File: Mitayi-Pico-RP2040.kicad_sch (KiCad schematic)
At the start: 53 parts, among them J1 EXP8, J2 USB_C_Receptacle_USB2.0, J3 Header_1, J4 Header_2, J5 SWD, J6 USB_B_Micro, SW1 Reset, SW2 UBUT, U1 W25Q128JVS, U2 MIC5219-3.3YM5, U3 RP2040, Y1 YIC-12M20P2/XT324-10/10

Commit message: Remove headers and much more
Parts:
- removed J1: EXP8, Connector_PinHeader_2.54mm:PinHeader_2x04_P2.54mm_Vertical, symbol Connector_Generic:Conn_02x04_Counter_Clockwise
- removed J3: Header_1, CIRCUITSTATE-Connector-Pin-Headers:PinHeader_1x20_2H_P2.54mm_Vertical, symbol Connector_Generic:Conn_01x20
- removed J4: Header_2, CIRCUITSTATE-Connector-Pin-Headers:PinHeader_1x20_2H_P2.54mm_Vertical, symbol Connector_Generic:Conn_01x20
- removed J5: SWD, Connector_PinHeader_2.54mm:PinHeader_1x03_P2.54mm_Vertical, symbol Connector_Generic:Conn_01x03
- removed J6: USB_B_Micro, Connector_USB:USB_Micro-B_Molex-105017-0001, symbol Connector:USB_B_Micro
- D1: footprint Diode_SMD:D_SOD-323_HandSoldering -> Diode_SMD:D_SOD-123F
- J2: JLC (none) -> C5337088
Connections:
- net +3V3: no longer U1.8 (VCC)
- net GND: no longer U1.4 (GND)
- net QSPI_SCLK: no longer U1.6 (CLK)
- net QSPI_SD0: no longer U1.5 (DI(IO0))
- net QSPI_SD1: no longer U1.2 (DO(IO1))
- net QSPI_SD2: no longer U1.3 (IO2)
- net QSPI_SD3: no longer U1.7 (IO3)
- net QSPI_SS: no longer U1.1 (~{CS})
- no-connect marks 3 -> 2
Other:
- note removed: "EXP8"
- note removed: "Headers"
- note removed: "Pads should be masked out if not using Micro-USB. Otherwise, USB-C connector will cause a short."
- note removed: "SWD"
- note removed: "USB Micro"
- moved on the sheet: U1

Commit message: Update footprints
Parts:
- J2: footprint CIRCUITSTATE_Connector_USB:Korean-Hroparts-Elec_TYPE-C-31-M-12 -> 00ProjectFootprints:Korean-Hroparts-Elec_TYPE-C-31-M-12
- U1: footprint Package_SO:SOIC-8_5.23x5.23mm_P1.27mm -> 00ProjectFootprints:SOIC-8_5.23x5.23mm_P1.27mm
- U3: footprint CIRCUITSTATE-QFN:RP2040-QFN-56 -> 00ProjectFootprints:RP2040-QFN-56
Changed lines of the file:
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@@
       (effects (font (size 0.8 0.8)))
     )
-    (property "Footprint" "CIRCUITSTATE_Connector_USB:Korean-Hroparts-Elec_TYPE-C-31-M-12" (at 240.792 96.52 0)
+    (property "Footprint" "00ProjectFootprints:Korean-Hroparts-Elec_TYPE-C-31-M-12" (at 240.792 96.52 0)
       (effects (font (size 0.8 0.8)) hide)
     )
@@
       (effects (font (size 0.8 0.8)))
     )
-    (property "Footprint" "Package_SO:SOIC-8_5.23x5.23mm_P1.27mm" (at 337.312 46.99 0)
+    (property "Footprint" "00ProjectFootprints:SOIC-8_5.23x5.23mm_P1.27mm" (at 337.312 46.99 0)
       (effects (font (size 0.8 0.8)) hide)
     )
@@
       (effects (font (size 0.8 0.8)))
     )
-    (property "Footprint" "CIRCUITSTATE-QFN:RP2040-QFN-56" (at 118.999 130.302 0)
-      (effects (font (size 0.8 0.8)) hide)
-    )
+    (property "Footprint" "00ProjectFootprints:RP2040-QFN-56" (at 118.999 130.302 0)
+      (effects (font (size 0.8 0.8)) hide)
+    )

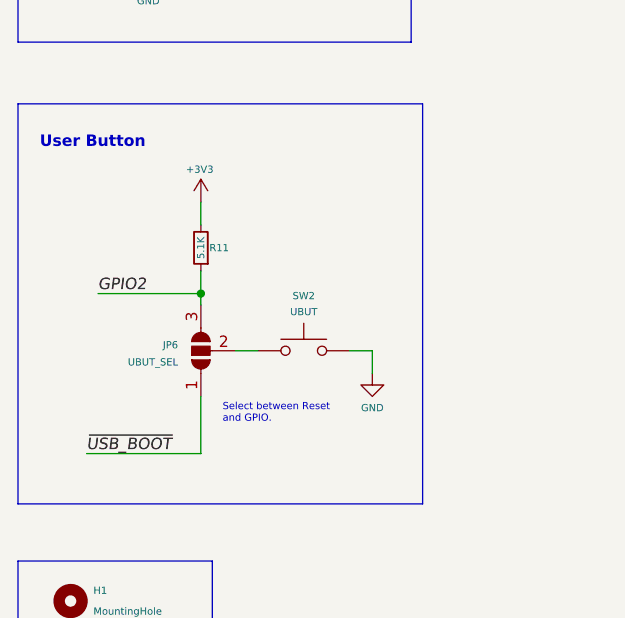
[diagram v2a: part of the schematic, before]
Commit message: Simplyfix Boot Button
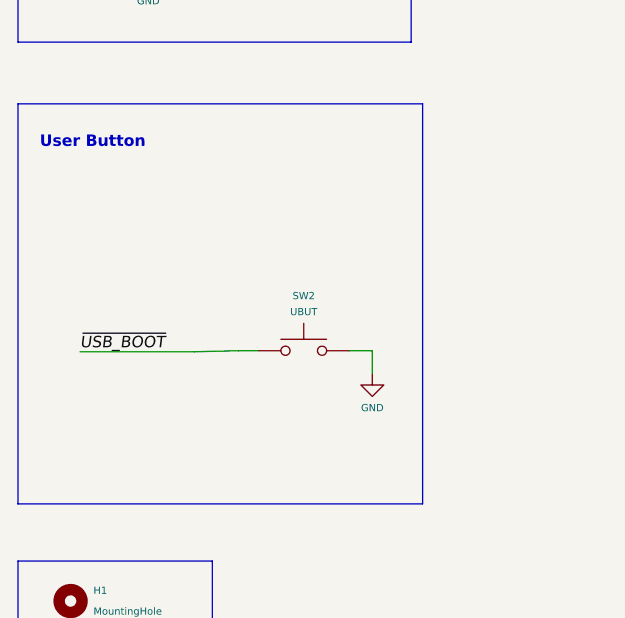
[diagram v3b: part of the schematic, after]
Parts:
- removed JP6: UBUT_SEL, CIRCUITSTATE_Jumper_SMD:Solder-Jumper_3P_Open_0402, symbol Jumper:SolderJumper_3_Open
- removed R11: 5.1K, Resistor_SMD:R_0402_1005Metric_Pad0.72x0.64mm_HandSolder, symbol Device:R_Small
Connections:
- net ~{USB_BOOT}: now also SW2.1
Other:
- note removed: "Select between Reset and GPIO."
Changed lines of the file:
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@@
   (junction (at 82.55 40.64) (diameter 1.016) (color 0 0 0 0)
-  )
-  (junction (at 41.402 223.012) (diameter 0) (color 0 0 0 0)
   )
   (junction (at 306.07 86.36) (diameter 1.016) (color 0 0 0 0)
@@
     (stroke (width 0) (type solid))
   )
-  (wire (pts (xy 29.972 223.012) (xy 41.402 223.012))
-    (stroke (width 0) (type default))
-  )
   (wire (pts (xy 322.072 34.29) (xy 322.072 33.02))
     (stroke (width 0) (type default))
@@
     (stroke (width 0) (type solid))
   )
-  (wire (pts (xy 45.212 229.362) (xy 47.752 229.362))
-    (stroke (width 0) (type default))
-  )
   (wire (pts (xy 174.752 35.052) (xy 174.752 36.322))
     (stroke (width 0) (type solid))
@@
     (stroke (width 0) (type default))
   )
-  (wire (pts (xy 41.402 220.472) (xy 41.402 223.012))
-    (stroke (width 0) (type default))
-  )
   (wire (pts (xy 266.7 81.28) (xy 272.542 81.28))
     (stroke (width 0) (type solid))
@@
     (stroke (width 0) (type solid))
   )
+  (wire (pts (xy 45.5995 229.362) (xy 47.752 229.362))
+    (stroke (width 0) (type default))
+  )
   (wire (pts (xy 154.432 45.212) (xy 154.432 46.482))
     (stroke (width 0) (type solid))
   )
-  (wire (pts (xy 28.702 240.792) (xy 41.402 240.792))
+  (wire (pts (xy 27.9773 229.4751) (xy 40.6773 229.4751))
     (stroke (width 0) (type default))
   )
@@
     (stroke (width 0) (type default))
   )
-  (wire (pts (xy 41.402 223.012) (xy 41.402 224.282))
-    (stroke (width 0) (type default))
-  )
-  (wire (pts (xy 41.402 212.852) (xy 41.402 215.392))
-    (stroke (width 0) (type default))
-  )
   (wire (pts (xy 154.432 43.942) (xy 154.432 45.212))
     (stroke (width 0) (type solid))
@@
     (stroke (width 0) (type default))
   )
-  (wire (pts (xy 41.402 240.792) (xy 41.402 234.442))
+  (wire (pts (xy 40.6773 229.4751) (xy 45.5995 229.362))
     (stroke (width 0) (type default))
   )
@@
     (effects (font (size 0.8 0.8)) (justify left bottom))
   )
-  (text "Select between Reset\nand GPIO." (at 43.815 237.49 0)
-    (effects (font (size 0.8 0.8)) (justify left bottom))
-  )
   (text "Flash Memory" (at 286.893 25.527 0)
     (effects (font (size 1.27 1.27) (thickness 0.254) bold) (justify left bottom))
@@
     (effects (font (size 1.27 1.27) italic) (justify right bottom))
   )
-  (label "GPIO2" (at 29.972 223.012 0) (fields_autoplaced)
-    (effects (font (size 1.27 1.27) italic) (justify left bottom))
-  )
   (label "GPIO23" (at 30.48 116.84 0) (fields_autoplaced)
     (effects (font (size 1.27 1.27) italic) (justify left bottom))
@@
     (effects (font (size 1.27 1.27) italic) (justify right bottom))
   )
-  (label "~{USB_BOOT}" (at 28.702 240.792 0) (fields_autoplaced)
+  (label "~{USB_BOOT}" (at 27.9773 229.4751 0) (fields_autoplaced)
     (effects (font (size 1.27 1.27) italic) (justify left bottom))
   )
@@
     )
   )
-  (symbol (lib_id "power:+3V3") (at 41.402 212.852 0) (unit 1)
-    (in_bom yes) (on_board yes) (dnp no)
-    (property "Reference" "#PWR036" (at 41.402 216.662 0)
-      (effects (font (size 0.8 0.8)) hide)
-    )
-    (property "Value" "+3V3" (at 41.275 209.2198 0)
-      (effects (font (size 0.8 0.8)))
-    )
-    (property "Footprint" "" (at 41.402 212.852 0)
-      (effects (font (size 0.8 0.8)) hide)
-    )
-    (property "Datasheet" "" (at 41.402 212.852 0)
-      (effects (font (size 0.8 0.8)) hide)
-    )
-    (pin "1")
-    (instances
-      (project "Mitayi-Pico-RP2040"
-        (path "/35c47459-45a7-4753-acae-c8b47e7575e1"
-          (reference "#PWR036") (unit 1)
-        )
-      )
-    )
-  )
   (symbol (lib_id "Device:C") (at 232.41 40.132 0) (unit 1)
     (in_bom yes) (on_board yes) (dnp no)
@@
     )
   )
-  (symbol (lib_id "Device:R_Small") (at 41.402 217.932 180) (unit 1)
-    (in_bom yes) (on_board yes) (dnp no)
-    (property "Reference" "R11" (at 43.434 217.932 0)
-      (effects (font (size 0.8 0.8)))
-    )
-    (property "Value" "5.1K" (at 41.402 217.932 90)
-      (effects (font (size 0.8 0.8)))
-    )
-    (property "Footprint" "Resistor_SMD:R_0402_1005Metric_Pad0.72x0.64mm_HandSolder" (at 41.402 217.932 0)
-      (effects (font (size 0.8 0.8)) hide)
-    )
-    (property "Datasheet" "~" (at 41.402 217.932 0)
-      (effects (font (size 0.8 0.8)) hide)
-    )
-    (pin "1")
-    (pin "2")
-    (instances
-      (project "Mitayi-Pico-RP2040"
-        (path "/35c47459-45a7-4753-acae-c8b47e7575e1"
-          (reference "R11") (unit 1)
-        )
-      )
-    )
-  )
   (symbol (lib_id "power:GND") (at 76.2 134.62 0) (unit 1)
     (in_bom yes) (on_board yes) (dnp no)
@@
         )
       )
-    )
-  )
-  (symbol (lib_id "Jumper:SolderJumper_3_Open") (at 41.402 229.362 90) (unit 1)
-    (in_bom yes) (on_board yes) (dnp no)
-    (property "Reference" "JP6" (at 38.862 228.7269 90)
-      (effects (font (size 0.8 0.8)) (justify left))
-    )
-    (property "Value" "UBUT_SEL" (at 38.862 230.6319 90)
-      (effects (font (size 0.8 0.8)) (justify left))
-    )
-    (property "Footprint" "CIRCUITSTATE_Jumper_SMD:Solder-Jumper_3P_Open_0402" (at 41.402 229.362 0)
-      (effects (font (size 0.8 0.8)) hide)
-    )
-    (property "Datasheet" "~" (at 41.402 229.362 0)
-      (effects (font (size 0.8 0.8)) hide)
-    )
-    (pin "1")
-    (pin "2")
-    (pin "3")
-    (instances
-      (project "Mitayi-Pico-RP2040"
-        (path "/35c47459-45a7-4753-acae-c8b47e7575e1"
-          (reference "JP6") (unit 1)
-        )
-      )

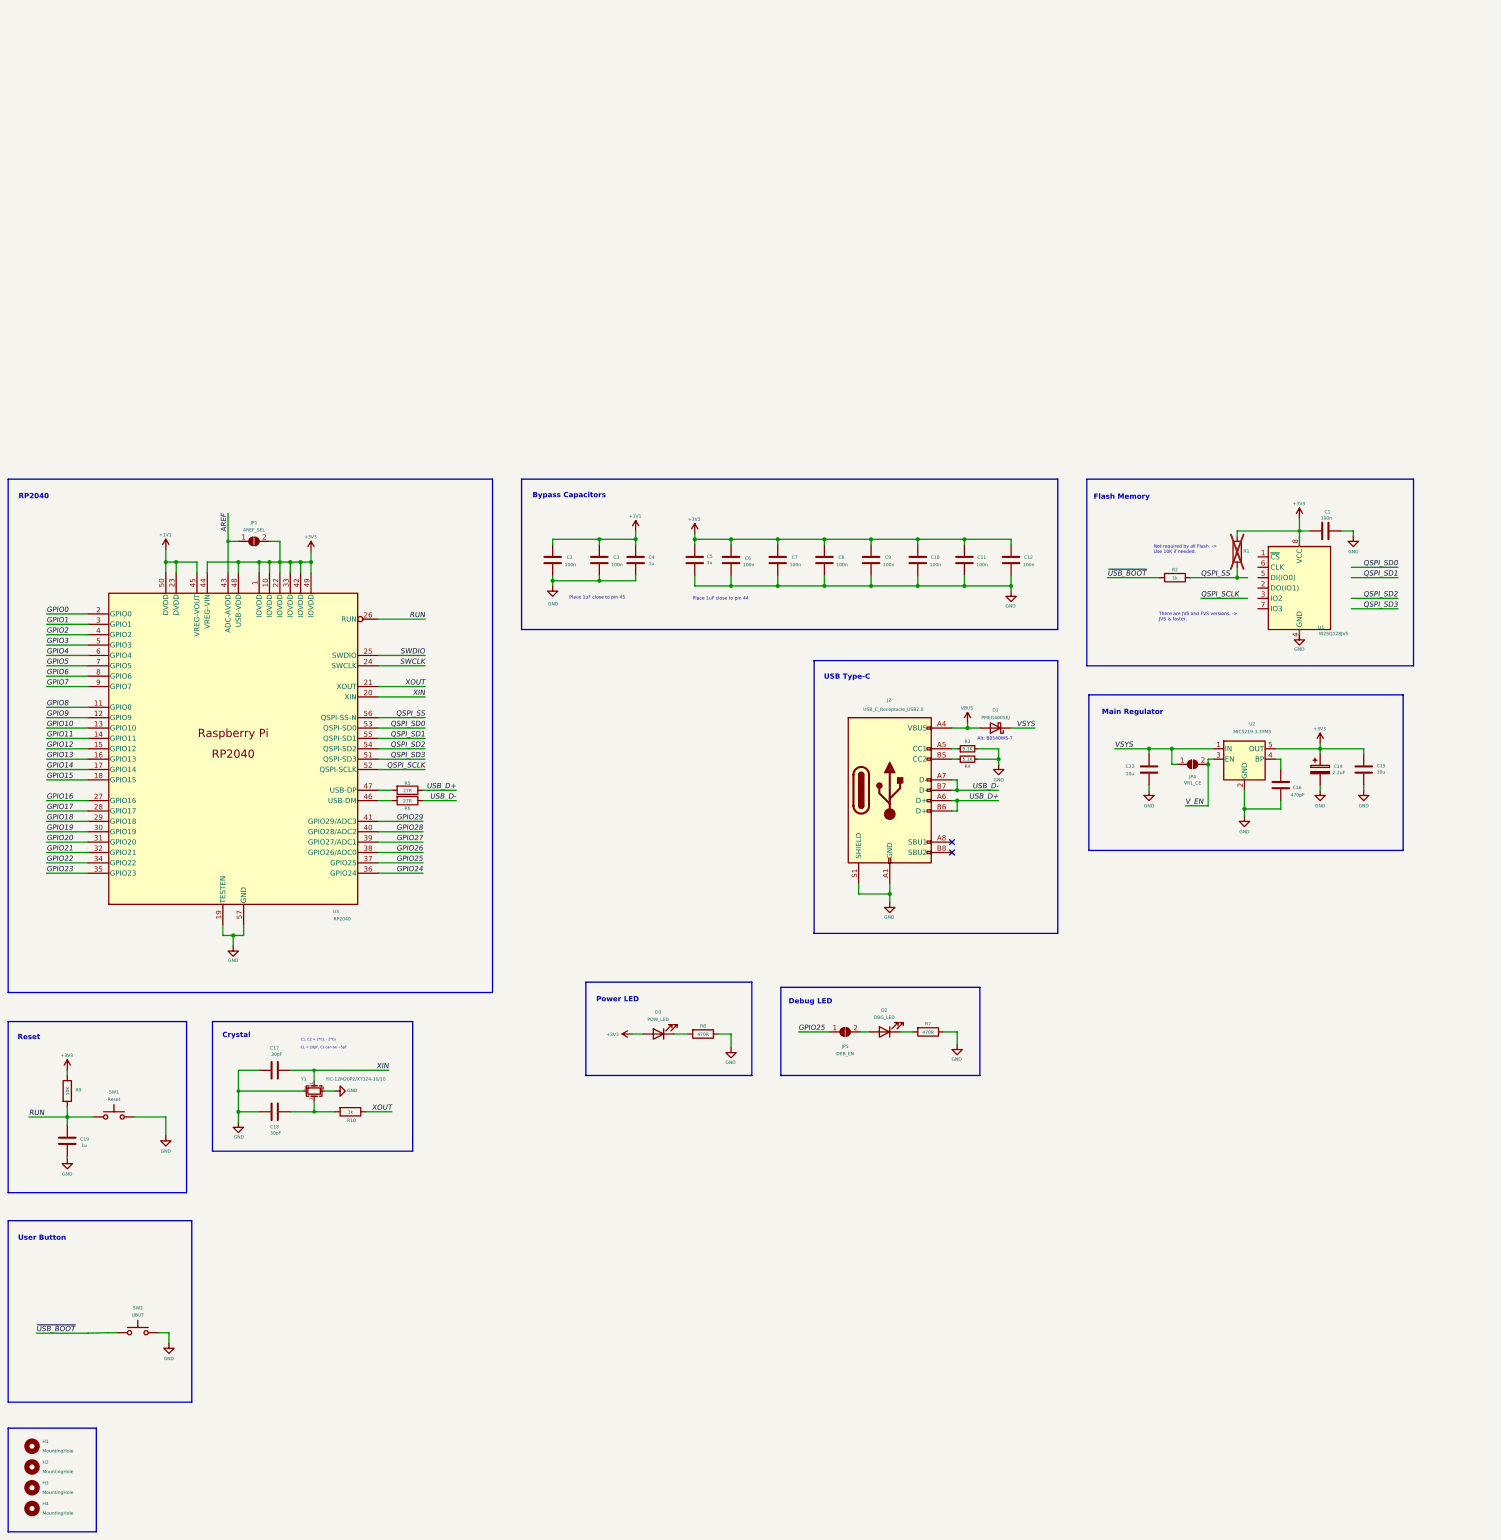
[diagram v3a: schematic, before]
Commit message: Added more components
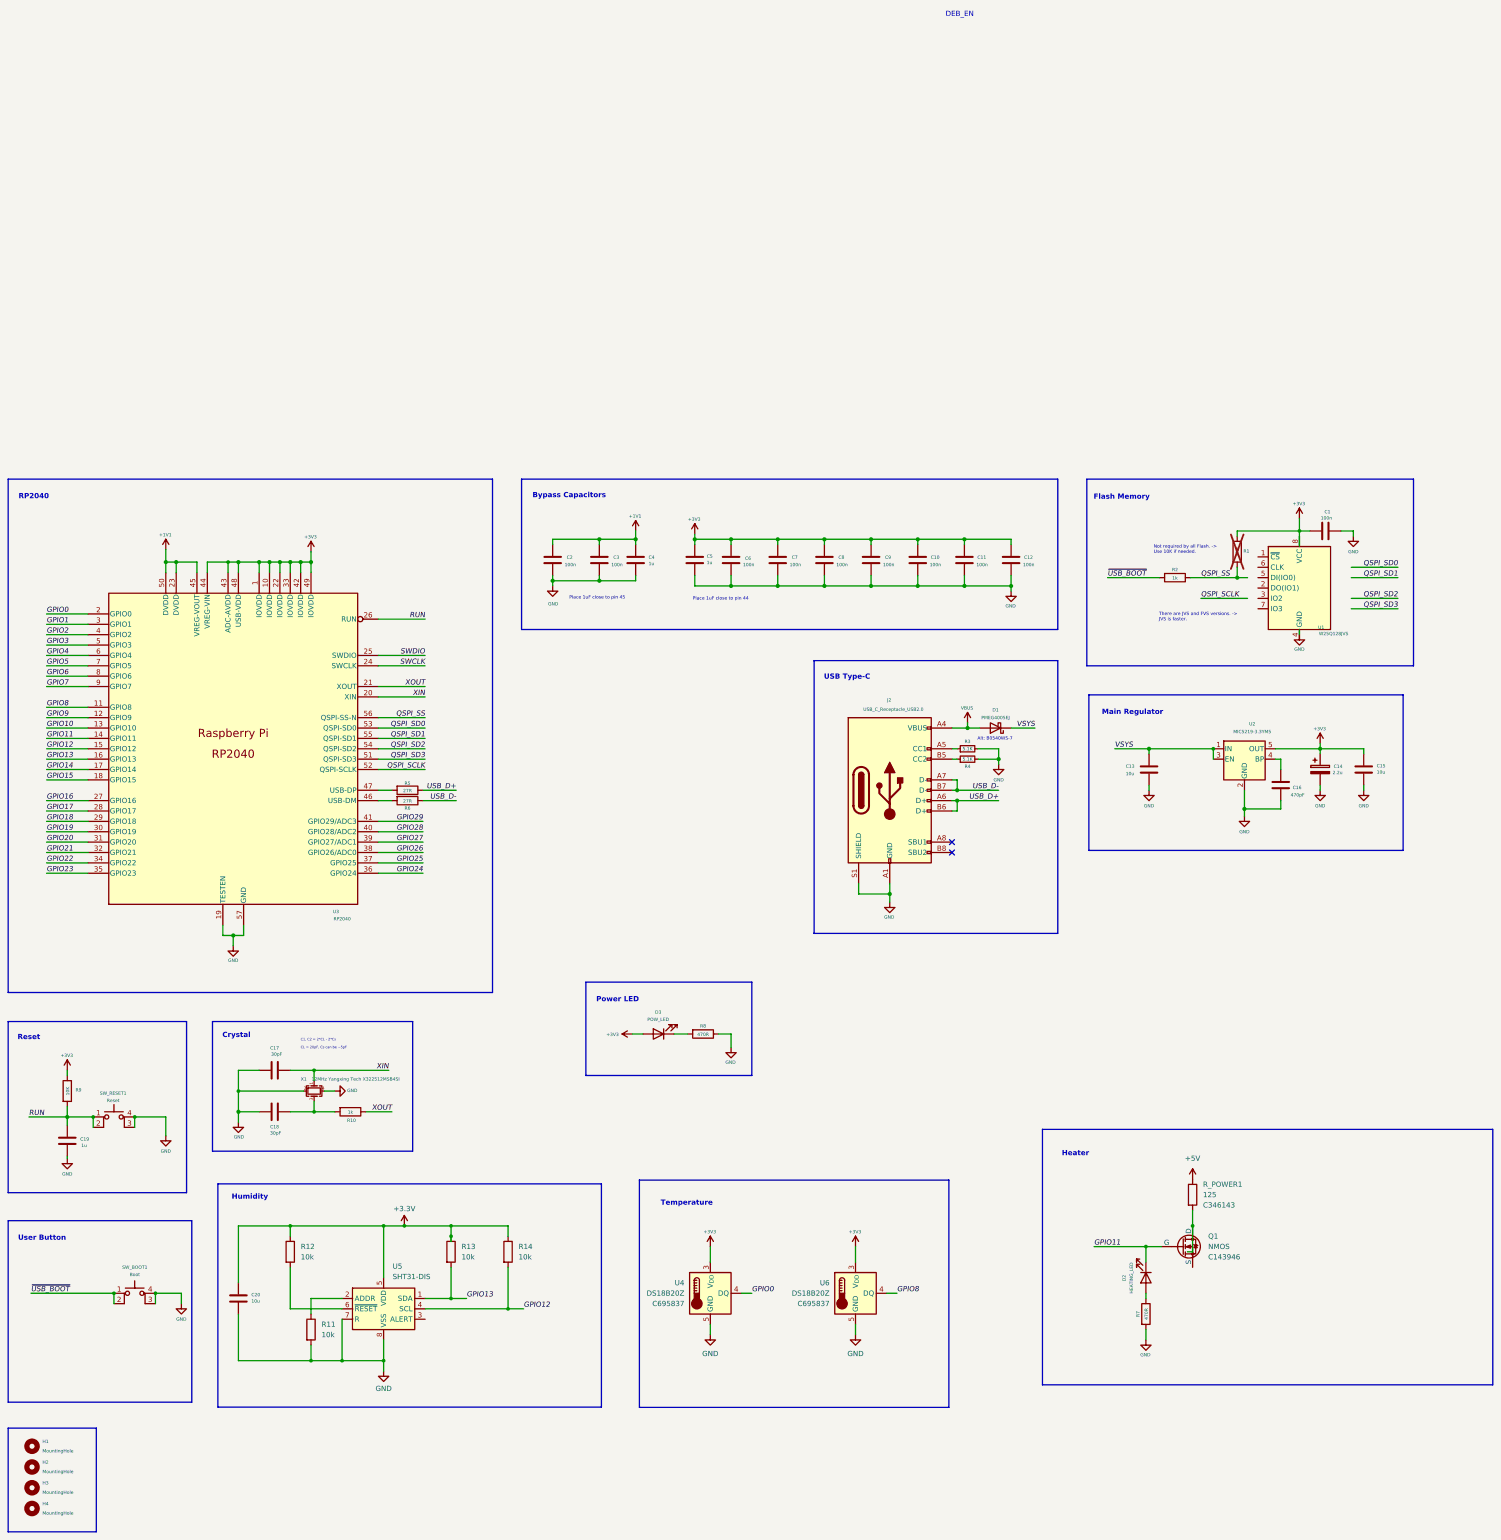
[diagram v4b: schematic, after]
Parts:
- removed JP1: AREF_SEL, CIRCUITSTATE_Jumper_SMD:Solder-Jumper_2P_Open_0402, symbol Jumper:SolderJumper_2_Open
- removed JP4: VR1_CE, CIRCUITSTATE_Jumper_SMD:Solder-Jumper_2P_Open_0402, symbol Jumper:SolderJumper_2_Open
- removed JP5: DEB_EN, CIRCUITSTATE_Jumper_SMD:Solder-Jumper_2P_Open_0402, symbol Jumper:SolderJumper_2_Open
- added C20: 10u, Capacitor_SMD:C_0603_1608Metric, symbol Device:C
- added Q1: NMOS, Package_TO_SOT_SMD:SOT-23, symbol 000_project_library:NMOS
- added R11, R12, R13, R14: 10k, Resistor_SMD:R_0402_1005Metric_Pad0.72x0.64mm_HandSolder, symbol Device:R
- added R_POWER1: 125, Resistor_SMD:R_1210_3225Metric, symbol 000_project_library:R_POWER
- added U4, U6: DS18B20Z, Package_SO:SOIC-8_3.9x4.9mm_P1.27mm, symbol 000_project_library:DS18B20Z
- added U5: SHT31-DIS, Sensor_Humidity:Sensirion_DFN-8-1EP_2.5x2.5mm_P0.5mm_EP1.1x1.7mm, symbol Sensor_Humidity:SHT31-DIS
- C14: value 2.2uF -> 2.2u; footprint Capacitor_Tantalum_SMD:CP_EIA-2012-12_Kemet-R -> Capacitor_SMD:C_0402_1005Metric; JLC (none) -> C12530
- D2: value DBG_LED -> HEATING_LED
- SW_BOOT1: renamed from SW2; value UBUT -> Boot; footprint CIRCUITSTATE_Switch_SMD:CK_SW_SPST_UK-B0273-SP25Y -> 00_Project:TS-1187A-B-A-B; symbol Switch:SW_Push -> Switch:SW_MEC_5E; JLC (none) -> C318884
- SW_RESET1: renamed from SW1; footprint CIRCUITSTATE_Switch_SMD:CK_SW_SPST_UK-B0273-SP25Y -> 00_Project:TS-1187A-B-A-B; symbol Switch:SW_Push -> Switch:SW_MEC_5E; JLC (none) -> C318884
- X1: renamed from Y1; value YIC-12M20P2/XT324-10/10 -> 12MHz Yangxing Tech X322512MSB4SI; JLC (none) -> C9002
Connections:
- net AREF is gone; now on net +3V3: U3.43 (ADC-AVDD)
- net V_EN is gone; now on net VSYS: U2.3 (EN)
- net +3V3: now also U4.3 (V_{DD}), U6.3 (V_{DD})
- net GND: now also R7.2, SW_BOOT1.3 (K), SW_BOOT1.4 (A), SW_RESET1.3 (K), SW_RESET1.4 (A), C20.2, R11.2, U4.5 (GND), U5.7 (R), U5.8 (VSS), U5.9 (VSS), U6.5 (GND); no longer R7.1, SW_BOOT1.2, SW_RESET1.2
- net GPIO0: now also U4.4 (DQ)
- net GPIO11: now also D2.1 (K), Q1.2 (G)
- net GPIO12: now also R14.2, U5.4 (SCL)
- net GPIO13: now also R13.2, U5.1 (SDA)
- net GPIO8: now also U6.4 (DQ)
- net RUN: now also SW_RESET1.2
- net ~{USB_BOOT}: now also SW_BOOT1.2
- net at D2.2 (A): now also R7.1
- new net: R11.1, U5.2 (ADDR)
- new net: R12.2, U5.6 (~{RESET})
- new net: Q1.1 (D), R_POWER1.2
- new net +3.3V: C20.1, R12.1, R13.1, R14.1, U5.5 (VDD)
- new net +5V: R_POWER1.1
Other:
- note added: "DEB_EN"
- note added: "Heater"
- note added: "Humidity"
- note added: "Temperature"
- note removed: "Debug LED"
- moved on the sheet: D2, R7
